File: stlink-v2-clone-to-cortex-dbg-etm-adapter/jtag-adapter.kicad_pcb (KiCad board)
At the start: 2 copper layers, 12.7 x 19.1 mm, 3 parts, among them J1 Conn_02x05_Odd_Even, J2 Conn_02x10_Odd_Even

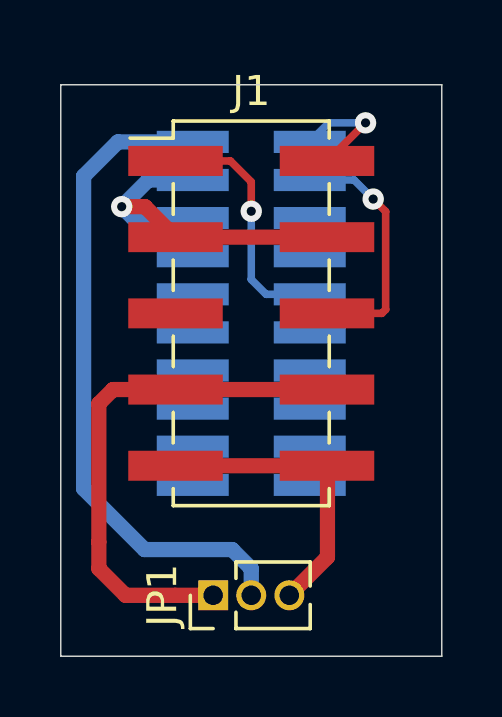
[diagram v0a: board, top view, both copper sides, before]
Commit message: [stlinkv2-jtagetm-adapter] Change header to socket for 20pin connector. Update README.
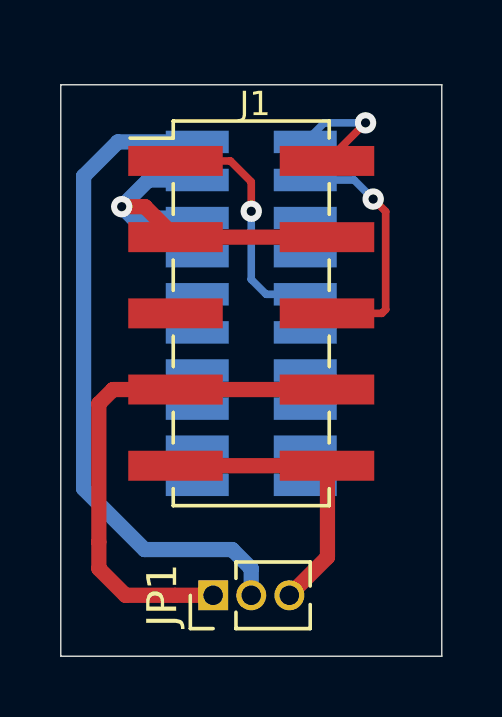
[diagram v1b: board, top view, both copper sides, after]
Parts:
- J2: footprint Connector_PinHeader_1.27mm:PinHeader_2x10_P1.27mm_Vertical_SMD -> Connector_PinSocket_1.27mm:PinSocket_2x10_P1.27mm_Vertical_SMD
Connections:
- J2 pad 1: /SWDIO -> Net-(J2-Pad1)
- J2 pad 10: Net-(J2-Pad10) -> /RST
- J2 pad 2: Net-(J2-Pad2) -> /SWDIO
- J2 pad 3: /SWCLK -> GND
- J2 pad 4: GND -> /SWCLK
- J2 pad 5: Net-(J2-Pad5) -> GND
- J2 pad 6: GND -> Net-(J2-Pad6)
- J2 pad 9: /RST -> Net-(J2-Pad9)
- JP1 pad 2: Net-(J2-Pad2) -> Net-(J2-Pad1)
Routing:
- net Net-(J2-Pad2): track 22.1 -> 0.00 mm
- net Net-(J2-Pad1): track 0.00 -> 22.1 mm
